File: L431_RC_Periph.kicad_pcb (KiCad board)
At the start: 4 copper layers, 19.5 x 17.5 mm, 55 parts, among them J1 CAN1, J2 BATT_C_MON, J3 RC IF, J4 BATT_V_MON, J5 Conn_ARM_SWD_TagConnect_TC203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, T1 Tab, T2 Tab, T3 Tab, T4 Tab, U1 PCB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

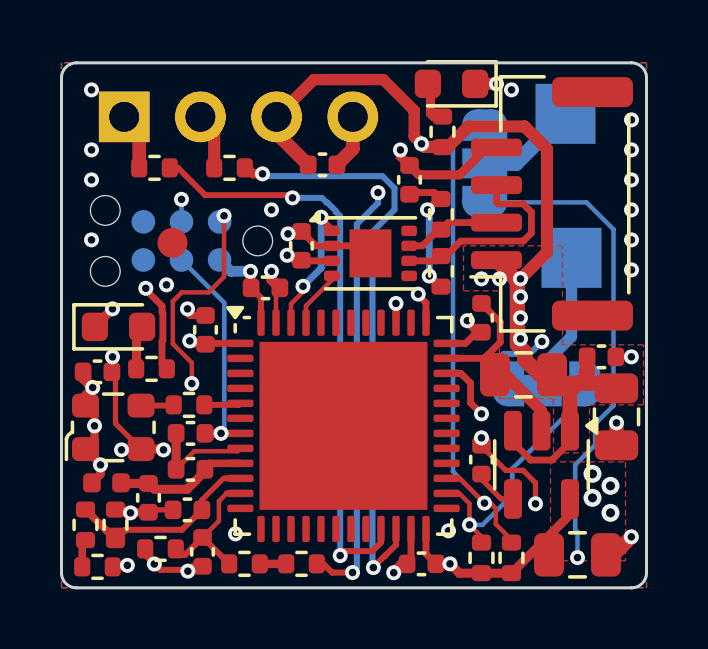
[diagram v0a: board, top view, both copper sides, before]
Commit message: Add JLC PCB DRU file from Kibot Custom DRU git repo
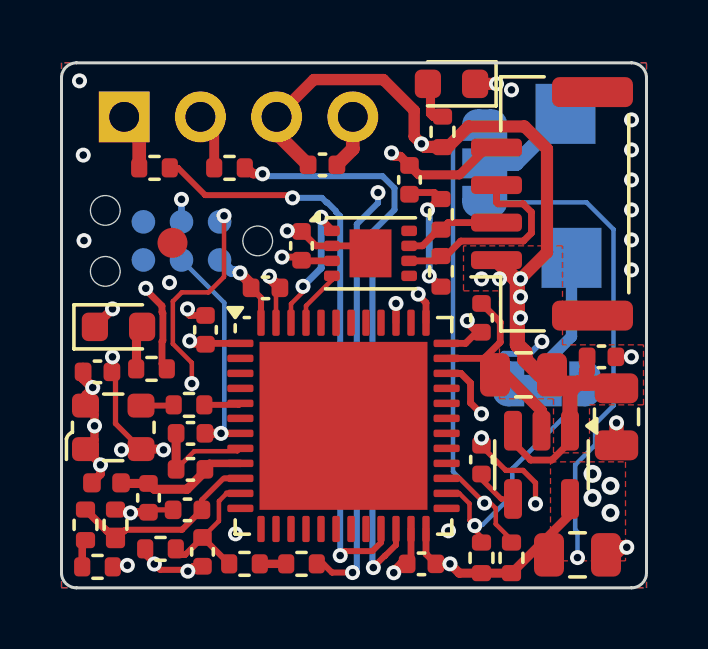
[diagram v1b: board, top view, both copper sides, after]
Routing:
- net +5V: track 40.8 -> 41.8 mm, vias 8 -> 7
- net GND: vias 32 -> 30

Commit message: Update to 6 pin headers and remove the two solder pads
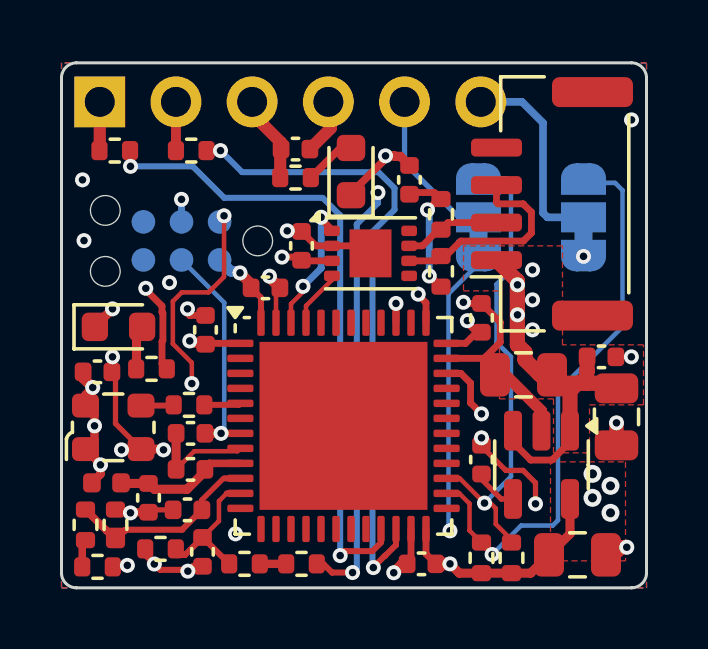
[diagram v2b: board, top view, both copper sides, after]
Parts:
- removed FID1: Fiducial, Fiducial:Fiducial_1mm_Mask2mm
- removed J2: BATT_C_MON, TestPoint:TestPoint_Pad_2.0x2.0mm
- removed J4: BATT_V_MON, TestPoint:TestPoint_Pad_2.0x2.0mm
- J3: footprint Connector_PinHeader_2.54mm:PinHeader_1x04_P2.54mm_Vertical -> Connector_PinHeader_2.54mm:PinHeader_1x06_P2.54mm_Vertical
- moved G*** 14.8 mm to (151.7, 78.5)
- moved JP2 5.68 mm to (151.4, 83.2), turned to 90 degrees
- moved R1 5.13 mm to (141.8, 81.9), turned to 180 degrees
- moved D1 4.45 mm to (143.7, 81.7), turned to 90 degrees
- moved JP1 1.81 mm to (147.9, 83.2)
- moved R6 1.44 mm to (135.8, 81.0)
- moved R7 1.40 mm to (138.3, 81.0)
- moved C7 1.04 mm to (141.8, 81.0)
- moved J3 0.96 mm to (135.3, 79.4)
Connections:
- JP1 pad 2: Net-(J4-Pin_1) -> /Out1
- JP2 pad 2: Net-(J2-Pin_1) -> /Out2
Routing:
- net +5V: track 41.8 -> 26.0 mm, vias 7 -> 6
- net Net-(JP1-A): track 32.9 -> 21.7 mm
- net /I2C2_SCL: track 8.76 -> 19.5 mm
- net /Out2: track 0.00 -> 6.78 mm
- net Net-(JP2-A): track 27.8 -> 22.2 mm
- net /Out1: track 0.00 -> 5.30 mm
- net Net-(J2-Pin_1): track 4.54 -> 0.00 mm
- net Net-(J4-Pin_1): track 3.87 -> 0.00 mm
- net GND: track 38.5 -> 36.5 mm, vias 30 -> 22
- net /USART3_TX: track 19.7 -> 21.6 mm
- net /USART3_RX: track 19.9 -> 21.4 mm
- net /I2C2_SDA: track 17.3 -> 16.2 mm
